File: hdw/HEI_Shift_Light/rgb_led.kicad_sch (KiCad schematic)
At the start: 13 parts

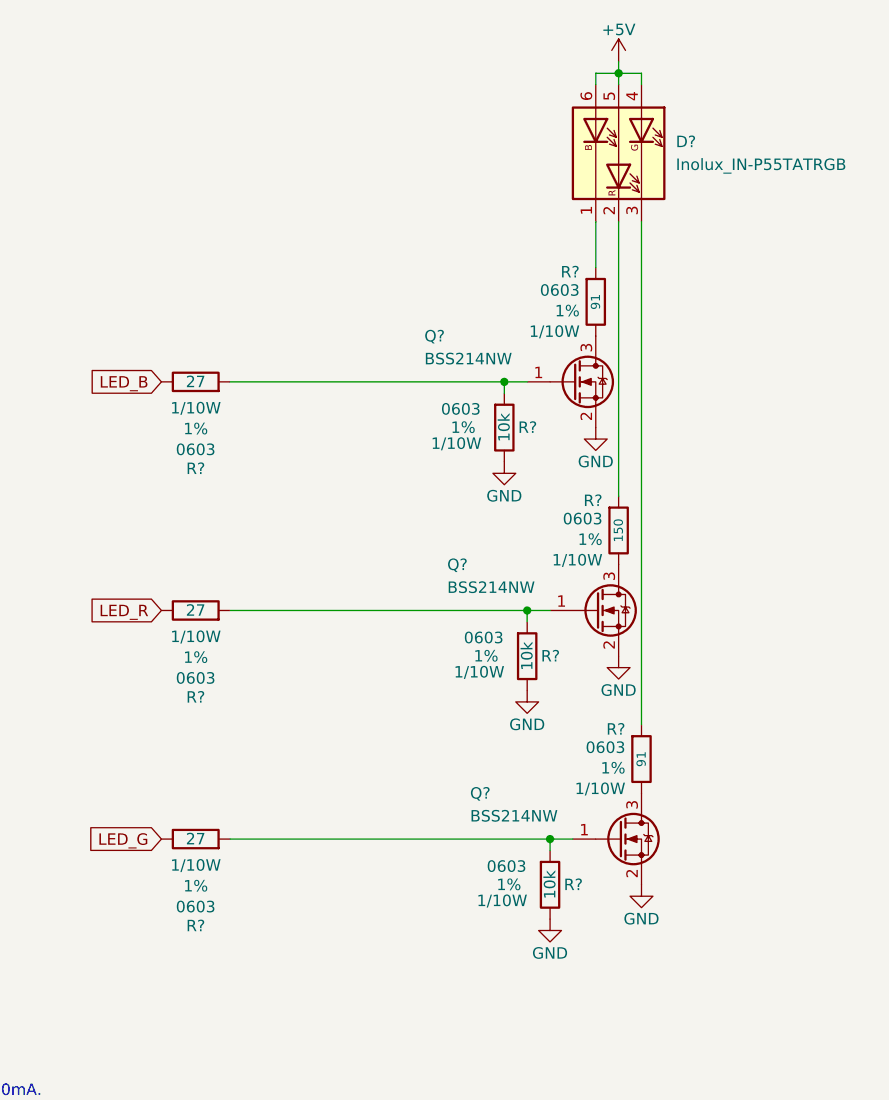
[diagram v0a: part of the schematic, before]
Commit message: filled in digikey part numbers
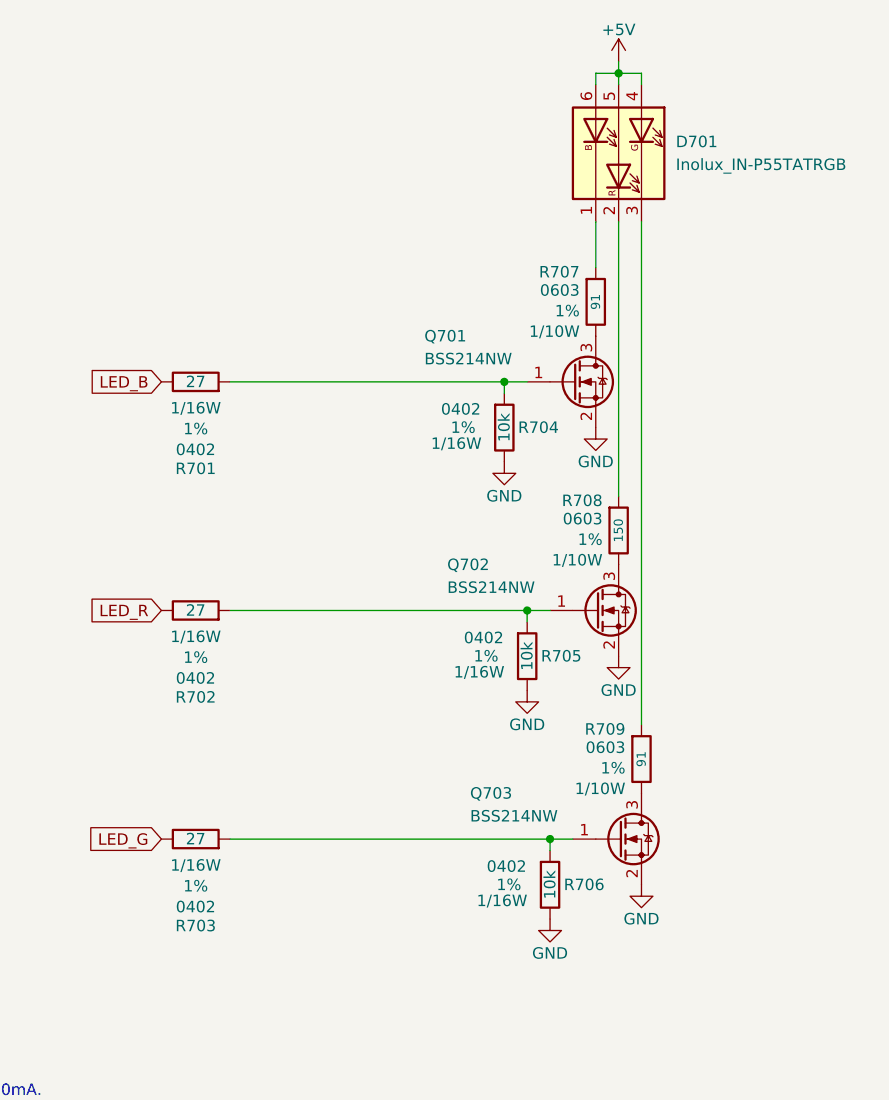
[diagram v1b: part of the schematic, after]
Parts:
- D701: renamed from D?; footprint LED_SMD:LED_Avago_PLCC4_3.2x2.8mm_CW -> LED_SMD:LED_Inolux_IN-P55TATRGB_PLCC6_5.0x5.5mm_P1.8mm; Digi-Key PN (none) -> 1830-1083-1-ND
- Q701, Q702, Q703: renamed from Q?; Digi-Key PN (none) -> BSS214NWH6327XTSA1CT-ND
- R701, R702, R703: renamed from R?; footprint Resistors_SMD:R_0603 -> Resistors_SMD:R_0402; Digi-Key PN 541-5306-1-ND -> 541-4082-1-ND; Wattage 1/10W -> 1/16W; display_footprint 0603 -> 0402
- R704, R705, R706: renamed from R?; footprint Resistors_SMD:R_0603 -> Resistors_SMD:R_0402; Digi-Key PN 541-10.0KHCT-ND -> 541-10.0KLCT-ND; Wattage 1/10W -> 1/16W; display_footprint 0603 -> 0402
- R707, R709: renamed from R?; footprint (none) -> Resistors_SMD:R_0603; Digi-Key PN (none) -> 541-CRCW060391R0FKEACCT-ND
- R708: renamed from R?; footprint (none) -> Resistors_SMD:R_0603; Digi-Key PN (none) -> 541-4023-1-ND

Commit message: cleaned up digikey pns
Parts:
- D701: Digi-Key PN 1830-1083-1-ND -> 1830-1098-1-ND
- Q701, Q702, Q703: value BSS214NW -> DMN3150LW-7; Digi-Key PN BSS214NWH6327XTSA1CT-ND -> DMN3150LWDICT-ND
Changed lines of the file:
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@@
 		(property "Intersheetrefs" "${INTERSHEET_REFS}"
 			(at 104.3601 106.68 0)
-			(hide yes)
 			(show_name no)
 			(do_not_autoplace no)
@@
 		(property "Intersheetrefs" "${INTERSHEET_REFS}"
 			(at 104.3601 132.08 0)
-			(hide yes)
 			(show_name no)
 			(do_not_autoplace no)
@@
 		(property "Intersheetrefs" "${INTERSHEET_REFS}"
 			(at 104.3601 81.28 0)
-			(hide yes)
 			(show_name no)
 			(do_not_autoplace no)
@@
 			)
 		)
-		(property "Value" "BSS214NW"
+		(property "Value" "DMN3150LW-7"
 			(at 147.32 129.54 0)
 			(show_name no)
@@
 			)
 		)
-		(property "Digi-Key PN" "BSS214NWH6327XTSA1CT-ND"
+		(property "Digi-Key PN" "DMN3150LWDICT-ND"
 			(at 163.83 132.08 0)
 			(hide yes)
@@
 			)
 		)
-		(property "Value" "BSS214NW"
+		(property "Value" "DMN3150LW-7"
 			(at 142.24 78.74 0)
 			(show_name no)
@@
 			)
 		)
-		(property "Digi-Key PN" "BSS214NWH6327XTSA1CT-ND"
+		(property "Digi-Key PN" "DMN3150LWDICT-ND"
 			(at 158.75 81.28 0)
 			(hide yes)
@@
 			)
 		)
-		(property "Digi-Key PN" "1830-1083-1-ND"
+		(property "Digi-Key PN" "1830-1098-1-ND"
 			(at 163.83 55.88 0)
 			(hide yes)
@@
 			)
 		)
-		(property "Value" "BSS214NW"
+		(property "Value" "DMN3150LW-7"
 			(at 144.78 104.14 0)
 			(show_name no)
@@
 			)
 		)
-		(property "Digi-Key PN" "BSS214NWH6327XTSA1CT-ND"
+		(property "Digi-Key PN" "DMN3150LWDICT-ND"
 			(at 161.29 106.68 0)
 			(hide yes)
